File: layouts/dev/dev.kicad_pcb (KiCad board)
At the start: 6 copper layers, 32.5 x 59.6 mm, 74 parts

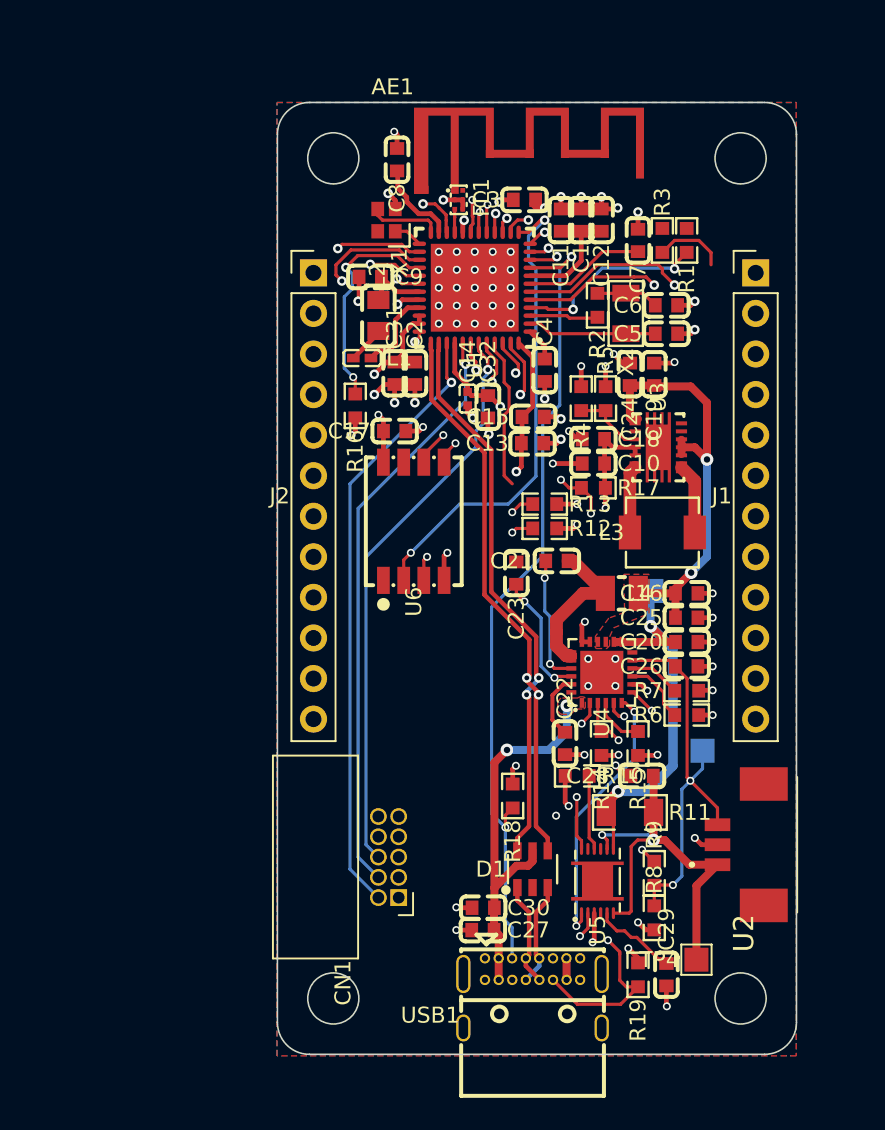
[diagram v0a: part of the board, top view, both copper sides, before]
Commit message: feat: put USART1, LPUART1, I2C1 and SPI1 on the headers
The chip sets the ceiling, not the header. STM32WB55CGUx.xml ends at I2C1,
I2C3, USART1, LPUART1, SPI1 and QUADSPI - there is no SPI2, no I2C2, no
USART2. The larger packages have SPI2, but its pins (PB12-PB15, PC2/PC3,
PD0-PD4) are not bonded out in UFQFPN-48.

QUADSPI is dead here too: QUADSPI_CLK exists only on PA3, and PA3 is the
only possible LPUART1_RX (the other, PA12, is USB D+); BK1_IO0 is PB9 and
BK1_IO1 is PB8, the PMIC bus. Turning it on would cost the second UART and
charger control at once.

Header real estate was 13 positions, not 9 - the left strip still had four
empty ones left over from SWD. Fourteen signals wanted them, so one had to
go, and PB5 is the one that loses nothing: LPUART1_TX is also on PA2,
SPI1_MOSI on PA7, USART1_CK on PA8. It gets the user LED instead.

  J2  5 SD_CLK  6 SD_MISO  8 SD_MOSI  9 EXT_CS
  J1  2 PA2  3 PA3  4 PA8  5 PA9  6 PA10  7 PMIC_SCL  8 PMIC_SDA
      9 PB6  10 PB7

I2C lands on J1-7/8 rather than J1-9/10 on purpose: PB6 and PB7 keep their
existing copper that way, costing 12 routed segments instead of 23.

SPI1 on the left strip is the SD NAND's own bus, and there was no choice -
SPI1_SCK exists only on PA1 (CC2), PA5 (SD_CLK) and PB3 (SWO), SPI1_MISO
only on PA6 (SD_MISO), PA11 (USB) and PB4 (GAUGE_INT). Not one free pin.
The external device gets its own CS on PA15, the only free SPI1_NSS.

The exposed I2C is the power-stack bus, with BQ25896 at 0x6B and BQ27441 at
0x55. There is no second one: I2C3 has a single pin per signal on this
package (SCL only PA7, SDA only PB4) and both are taken. Consequences are
written down in headers.ato - the 0x6B clash with ST IMUs, the 40 s I2C
watchdog that drops the charger back to 500 mA, and the 4.7k pull-ups that
are sized for the board, not for 20 cm of wire.

PA8/PA9/PA10 sit together so USART1 can run synchronous as a second SPI
master without rewiring - firmware choice, not a solder choice.

Verified: ato build clea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
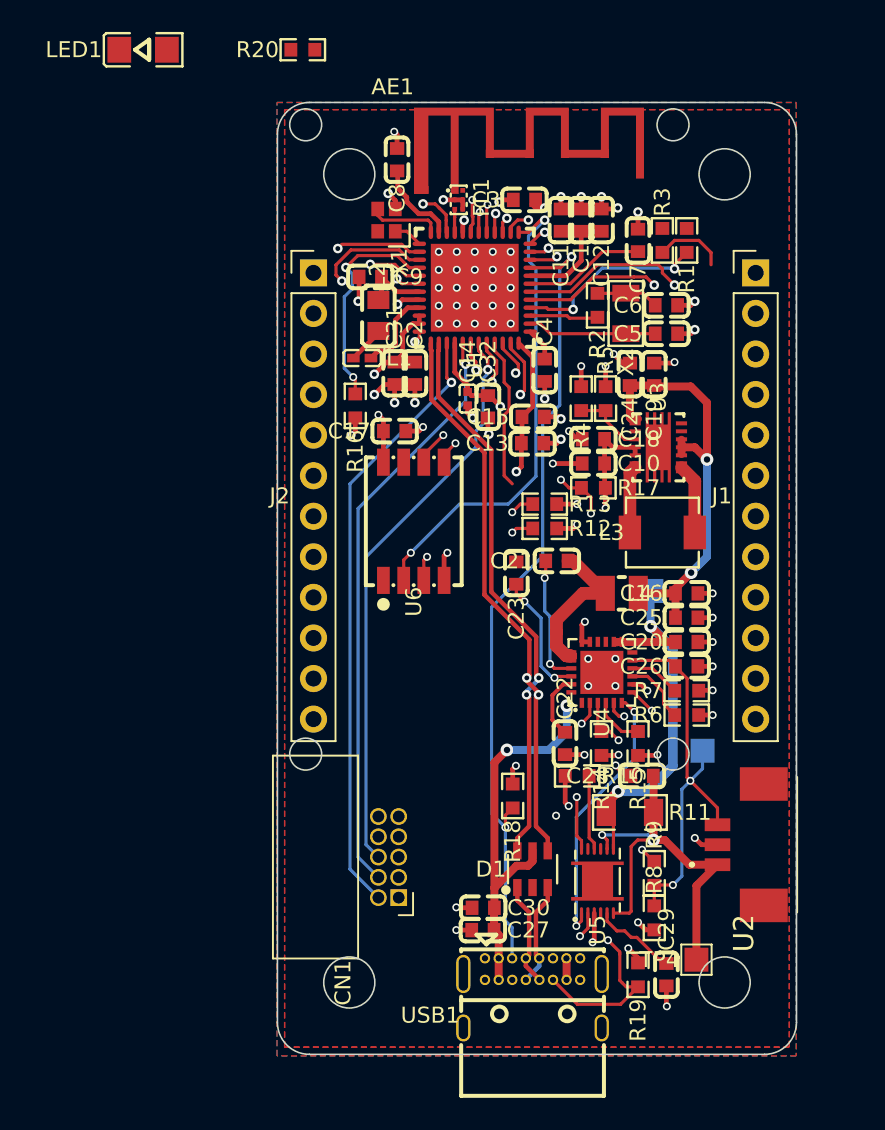
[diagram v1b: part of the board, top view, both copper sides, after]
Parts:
- added LED1: , Foshan_NationStar_Optoelectronics_NCD1206R1:LED1206-R-RD_RED, F.Cu at (0.00, 0.00)
- added R20: 1kΩ ±1%, UNI_ROYAL_0603WAF1001T5E:R0603, F.Cu at (10.0, 0.00)
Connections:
- J1 pad 7: PA15 -> PMIC_SCL
- J1 pad 8: PB5 -> PMIC_SDA
- J2 pad 5: 5 -> SD_CLK
- J2 pad 6: 6 -> SD_MISO
- J2 pad 8: 8 -> SD_MOSI
- J2 pad 9: 9 -> EXT_CS
- U1 pad 42: PA15 -> EXT_CS
- U1 pad 45: PB5 -> LED
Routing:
- net PB5: track 9.52 -> 0.00 mm
- net LED: track 0.00 -> 9.52 mm
- net PA15: track 1.83 -> 0.00 mm, vias 1 -> 0
- net EXT_CS: track 0.00 -> 1.83 mm, vias 0 -> 1
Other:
- outline, holes or cut-outs redrawn

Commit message: feat: add RESET and BOOT0 buttons and a TCA9534 I/O expander
The two system buttons cost nothing and fix the two most common physical
operations on the board. NRST and BOOT0 are not GPIO, so no pin is spent,
and both switches hang on nets that already have names - they introduce no
new net at all. Resetting used to mean shorting header pins or cutting
power; DFU meant a wire from J2-11 to J2-3. Now it is hold BOOT0, tap
RESET.

No series resistor on RESET, deliberately: the switch discharges the 100 nF
through its contacts, which erodes them slowly, but AN2586 and every Nucleo
and Discovery wire that button directly, and departing from a convention on
a board meant to feel familiar costs more than worn contacts. The switch is
rated 50 mA and 100 000 cycles. Its shield pin goes to ground - left
floating it collects charge from a finger and dumps it into the signal,
which on RESET means a board that resets when touched nearby.

The expander is TCA9534PWR (TSSOP-16, C783615, 28 799 in stock), picked on
three datasheet numbers: push-pull outputs, so an LED can sit to ground and
light on a high level instead of PCF8574's inverted logic; 1.65-5.5 V; and
0.9 uA standby. That last one is what killed the addressable RGB idea - a
WS2812 controller draws about 1 mA even dark, a thousand times this whole
chip. It sits at 0x20, clear of the charger at 0x6B and the gauge at 0x55.

  P0 red LED      P4 user button 1
  P1 green LED    P5 10k to ground (spare)
  P2 red LED      P6 10k to ground (spare)
  P3 user button  P7 10k to ground (spare)

nINT is open drain and gets its own 10k, landing on PB5 - the pin freed
during bus planning. An interrupt input needs no alternate function and PB5
has no useful one, so the pair is exact.

Buttons need external pull-ups because the TCA9534 has none (±1 uA input
current), unlike the PCF8574. Spare ports get pull-downs rather than a wire
to ground: a firmware mistake that drives them high becomes 330 uA instead
of shorting an output the datas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
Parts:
- added C33: 100nF ±10%, YAGEO_CC0603KRX7R9BB104:C0603, F.Cu at (80.0, -20.0)
- added LED2: , Foshan_NationStar_Optoelectronics_NCD1206R1:LED1206-R-RD_RED, F.Cu at (50.0, 0.00)
- added LED3: , Foshan_NationStar_Optoelectronics_NCD1206R1:LED1206-R-RD_RED, F.Cu at (30.0, 0.00)
- added R21: 10kΩ ±1%, YAGEO_RC0603FR_0710KL:R0603, F.Cu at (80.0, -10.0)
- added R22: 10kΩ ±1%, YAGEO_RC0603FR_0710KL:R0603, F.Cu at (80.0, -30.0)
- added R23: 1kΩ ±1%, UNI_ROYAL_0603WAF1001T5E:R0603, F.Cu at (80.0, -40.0)
- added R24: 1kΩ ±1%, UNI_ROYAL_0603WAF1001T5E:R0603, F.Cu at (80.0, -60.0)
- added R25: 1kΩ ±1%, UNI_ROYAL_0603WAF1001T5E:R0603, F.Cu at (80.0, -50.0)
- added R26: 10kΩ ±1%, YAGEO_RC0603FR_0710KL:R0603, F.Cu at (80.0, -70.0)
- added R27: 10kΩ ±1%, YAGEO_RC0603FR_0710KL:R0603, F.Cu at (80.0, -80.0)
- added R28: 10kΩ ±1%, YAGEO_RC0603FR_0710KL:R0603, F.Cu at (80.0, -90.0)
- added SW1: , C_K_KMR221GLFS:KEY-SMD_KMR2XXGXXX, F.Cu at (10.0, 0.00)
- added SW2: , C_K_KMR221GLFS:KEY-SMD_KMR2XXGXXX, F.Cu at (0.00, 0.00)
- added SW3: , C_K_KMR221GLFS:KEY-SMD_KMR2XXGXXX, F.Cu at (60.0, 0.00)
- added SW4: , C_K_KMR221GLFS:KEY-SMD_KMR2XXGXXX, F.Cu at (70.0, 0.00)
- added U7: , Texas_Instruments_TCA9534PWR:TSSOP-16_L5.0-W4.4-P0.65-LS6.4-BL, F.Cu at (20.0, 0.00)
- LED1: footprint Foshan_NationStar_Optoelectronics_NCD1206R1:LED1206-R-RD_RED -> Foshan_NationStar_Optoelectronics_NCD1206C1:LED1206-RD
- R20: value 1kΩ ±1% -> 10kΩ ±1%; footprint UNI_ROYAL_0603WAF1001T5E:R0603 -> YAGEO_RC0603FR_0710KL:R0603
- moved R20 70.0 mm to (80.0, 0.00)
- moved LED1 40.0 mm to (40.0, 0.00)
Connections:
- LED1 pad 1: A -> GND
- LED1 pad 2: GND -> LED1_A
- R20 pad 1: LED -> +3V3
- R20 pad 2: A -> BTN_USR0
- U1 pad 45: LED -> EXP_INT
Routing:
- net LED: track 9.52 -> 0.00 mm
- net EXP_INT: track 0.00 -> 9.52 mm

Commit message: refactor: swap the TSSOP-16 expander for a 3x3 QFN
The TCA9534 in TSSOP-16 measured 5.86 x 7.47 mm on the board - 43.7 mm2 of
courtyard on a board whose largest free block is 13 x 8.5 mm. TCA6408A in
VQFN-16 does the same job in 3.56 x 3.83 mm, or 13.6 mm2. Less than a
third, and nothing is given up: still 8 I/O, still an interrupt, still
push-pull outputs, still 1.65-5.5 V.

The 4-bit alternative in VSSOP-8 (PCA9536) would have saved slightly more
once its spare pull-downs are counted, but at the cost of half the I/O and
the interrupt entirely. The QFN keeps the whole design and costs only the
package style, which is the same 0.5 mm pitch as the MCU already on this
board.

Three things the QFN needs that the TSSOP did not, none of them an extra
part:

  * two supplies - VCCI feeds the I2C side, VCCP the P-ports, and the part
    can translate between them. Both go to +3V3 here. They are pins 14 and
    15, adjacent, so one 100 nF still covers both.
  * a RESET pin. The datasheet says to pull it up to VCCI "if no active
    connection is used"; a resistor only earns its place if something can
    pull the line down, and nothing here can. Tied straight to the rail.
  * an exposed pad, which the datasheet requires to be soldered. It goes to
    ground and board_setup stitches it like the others - one via in the
    1.70 x 1.70 pad, which is all that fits at 0.25 mm margin. For a part
    drawing 1.5 uA that pad is a ground anchor, not a heat path.

One address pin instead of three, so 0x20 and 0x21 rather than 0x20-0x27.
With a single expander that constrains nothing.

atopile's own stock lookup reports 3212 for C181499 where the LCSC product
page showed 14918 - the same split between warehouses seen earlier with the
gauge. Either figure is ample here, but the number to trust before ordering
is the one on the LCSC page.

Verified: ato build clean, check_pinout passes, clearance violations 60
before and 60 after - and the four shorting_items are gone, because the
small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
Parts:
- U7: footprint Texas_Instruments_TCA9534PWR:TSSOP-16_L5.0-W4.4-P0.65-LS6.4-BL -> Texas_Instruments_TCA6408ARGTR:QFN-16_L3.0-W3.0-P0.50-BL-EP1.7
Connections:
- R26 pad 1: 10 -> 8
- R27 pad 1: 11 -> 9
- R28 pad 1: 12 -> 10
- U7 pad 1: GND -> 10
- U7 pad 10: 10 -> EXP_LED1
- U7 pad 11: 11 -> EXP_LED2
- U7 pad 12: 12 -> BTN_USR0
- U7 pad 13: EXP_INT -> GND
- U7 pad 14: PMIC_SCL -> BTN_USR1
- U7 pad 15: PMIC_SDA -> 8
- U7 pad 2: GND -> EXP_INT
- U7 pad 3: GND -> PMIC_SCL
- U7 pad 4: EXP_LED0 -> PMIC_SDA
- U7 pad 5: EXP_LED1 -> +3V3
- U7 pad 6: EXP_LED2 -> +3V3
- U7 pad 7: BTN_USR0 -> GND
- U7 pad 8: GND -> 9
- U7 pad 9: BTN_USR1 -> EXP_LED0
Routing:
- net GND: vias 77 -> 78
